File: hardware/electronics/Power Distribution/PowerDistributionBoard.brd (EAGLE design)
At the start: 128.3 x 50.8 mm, 74 parts, among them IC1 LM556D, IC2 74AHC1G02DBV, IC3 74AHC1G02DBV, K1 EC2-12TNU, U1 IPS6041G, U2 IPS6041G, U3 V_REG_317SMD

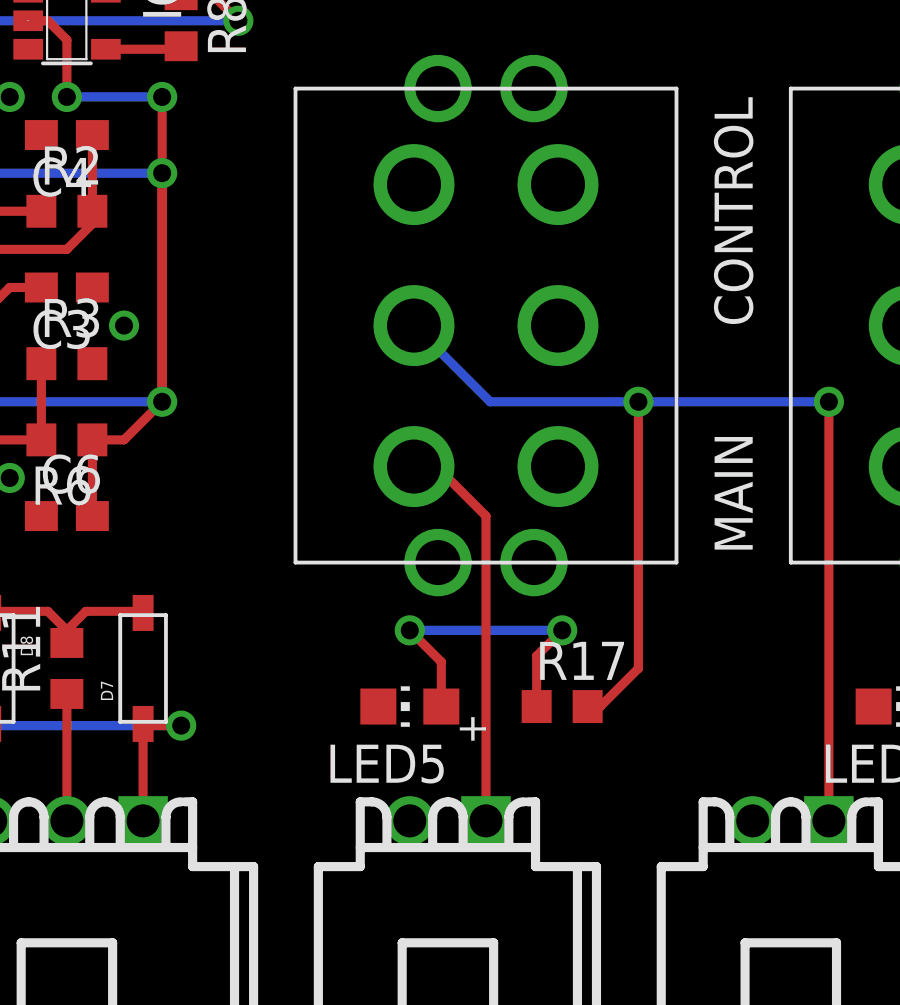
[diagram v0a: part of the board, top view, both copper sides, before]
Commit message: Changed the R/C input over to SBUS. Updates to the PowerDistributionBaord
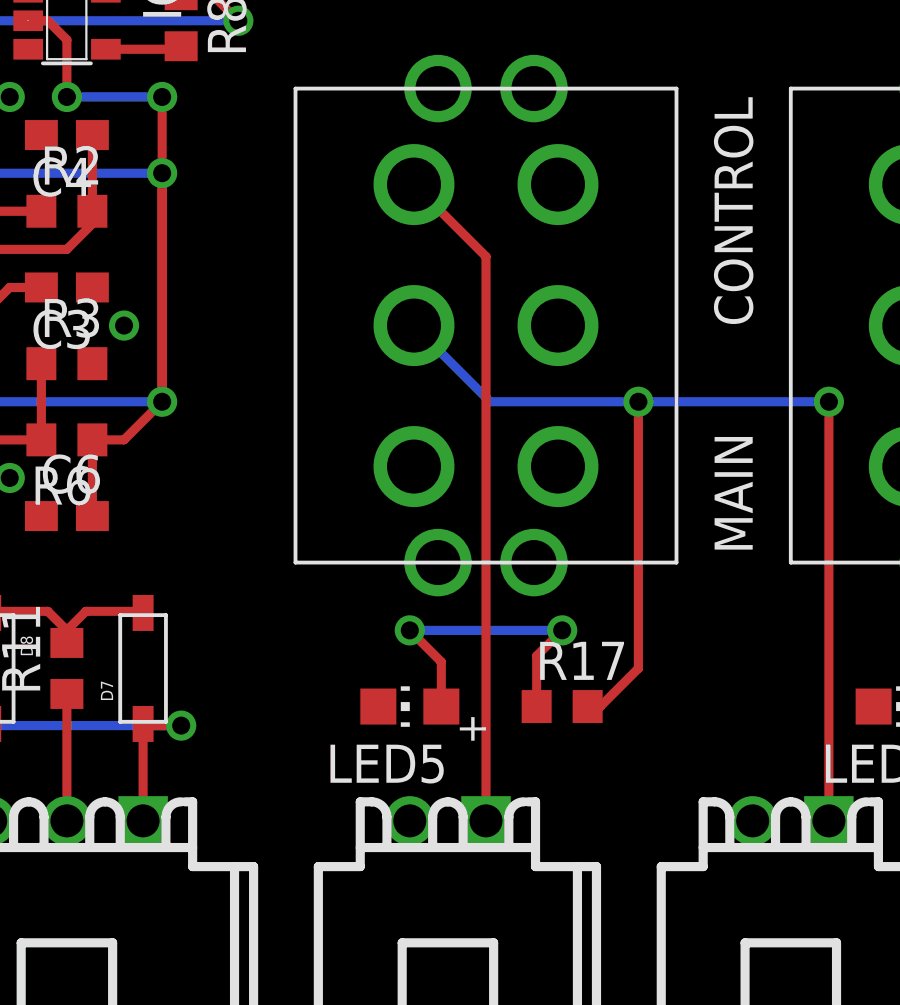
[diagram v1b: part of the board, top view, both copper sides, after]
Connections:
- net GND: now also CONTROL.3, CONTROL.6, HORN.3, HORN.6, MAIN.1, MAIN.6, MOTOR.3, MOTOR.6
- net N$34: now also MAIN.3; no longer MAIN.1
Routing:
- net N$34: track 13.2 -> 22.2 mm
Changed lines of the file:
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@@
 <contactref element="U3" pad="1"/>
 <contactref element="C10" pad="2"/>
-<contactref element="MAIN" pad="4"/>
 <contactref element="HORN" pad="4"/>
 <contactref element="CONTROL" pad="4"/>
@@
 <via x="51.435" y="30.48" extent="1-16" drill="0.6"/>
 <via x="47.625" y="25.4" extent="1-16" drill="0.6"/>
+<contactref element="MAIN" pad="6"/>
+<contactref element="CONTROL" pad="6"/>
+<contactref element="CONTROL" pad="3"/>
+<contactref element="MAIN" pad="4"/>
+<contactref element="MAIN" pad="1"/>
+<contactref element="MOTOR" pad="3"/>
+<contactref element="MOTOR" pad="6"/>
+<contactref element="HORN" pad="3"/>
+<contactref element="HORN" pad="6"/>
 </signal>
 <signal name="+5V">
@@
 </signal>
 <signal name="N$34">
-<contactref element="MAIN" pad="1"/>
 <contactref element="AUX-PWR" pad="P$1"/>
-<wire x1="63.5" y1="13.97" x2="63.5" y2="24.13" width="0.3048" layer="1"/>
-<wire x1="61.1" y1="25.78" x2="61.85" y2="25.78" width="0.3048" layer="1"/>
-<wire x1="61.85" y1="25.78" x2="63.5" y2="24.13" width="0.3048" layer="1"/>
+<wire x1="63.5" y1="13.97" x2="63.5" y2="32.78" width="0.3048" layer="1"/>
+<contactref element="MAIN" pad="3"/>
+<wire x1="63.5" y1="32.78" x2="61.1" y2="35.18" width="0.3048" layer="1"/>
 </signal>
 </signals>

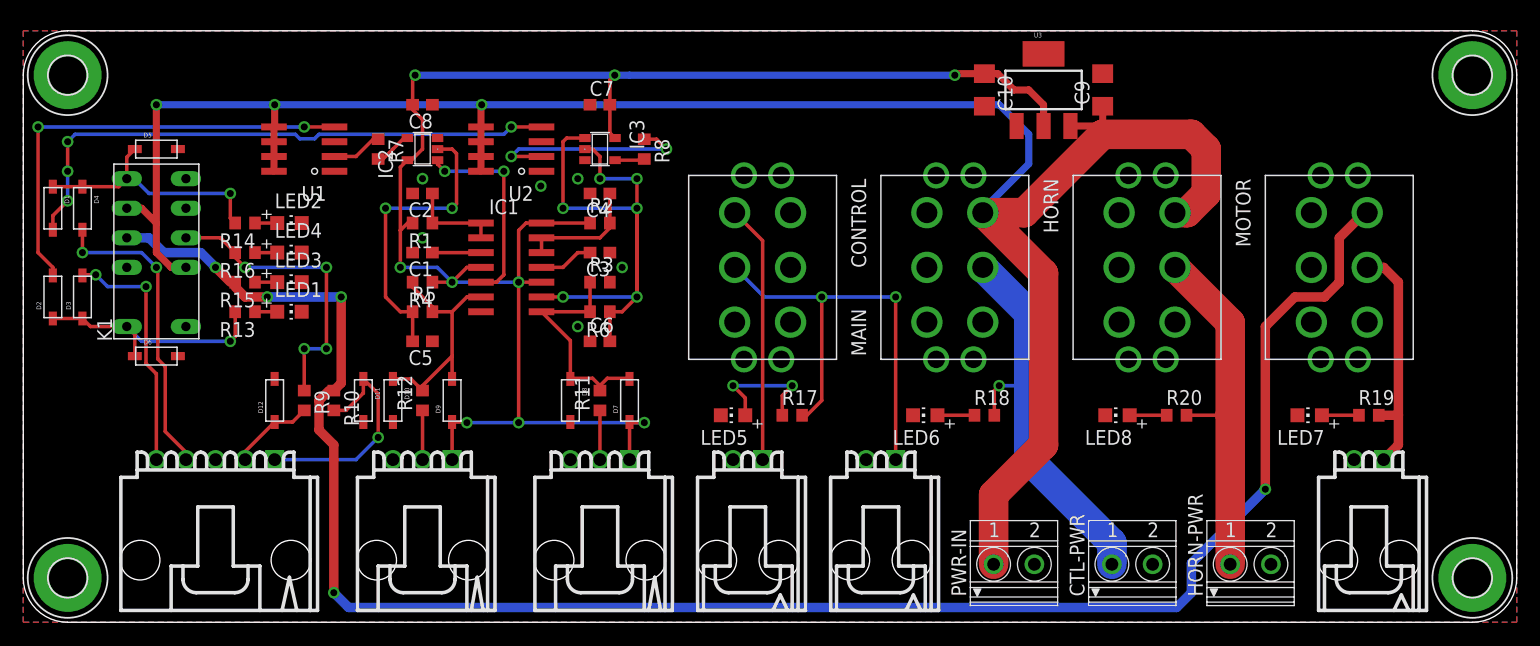
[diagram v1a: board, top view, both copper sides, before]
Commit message: Making sure we have the latest board in github
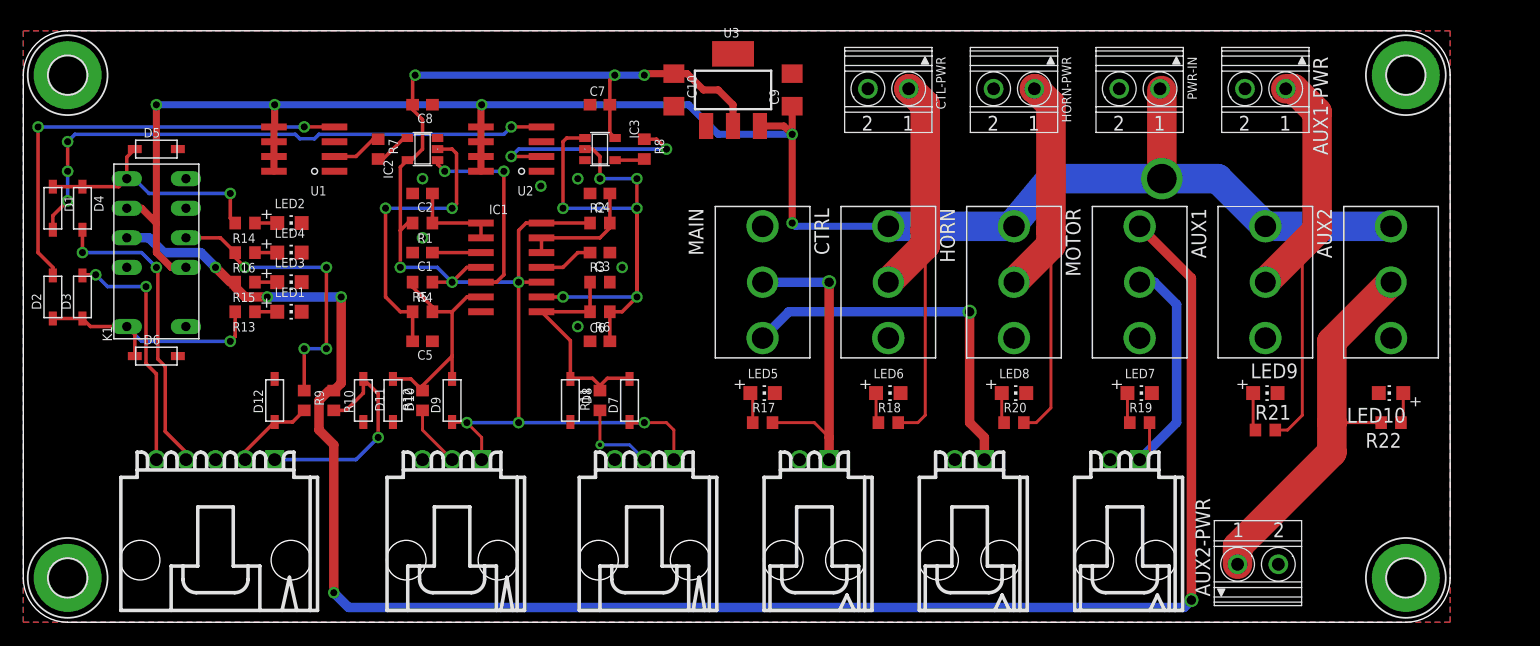
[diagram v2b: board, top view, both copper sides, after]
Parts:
- removed CONTROL: M20-DPDT, logos-switch:M20****13*
- added AUX1, AUX2, CTRL: M20-SPDT, logos-switch:M20-SPDT
- added AUX1-PWR, AUX2-PWR: 1751248, con-phoenix-350:1751248
- added LED10, LED9: (no value), adafruit:CHIP-LED0805
- added R21, R22: (no value), resistor:R0603
- HORN, MAIN, MOTOR: value M20-DPDT -> M20-SPDT; device logos-switch:M20****13* -> logos-switch:M20-SPDT
- moved CTL-PWR 45.7 mm to (74.3, 45.7), turned to 180 degrees
- moved HORN-PWR 45.4 mm to (85.1, 45.7), turned to 180 degrees
- moved PWR-IN 42.0 mm to (95.9, 45.7), turned to 180 degrees
- moved C10 26.7 mm to (55.9, 45.7)
- moved U3 26.7 mm to (61.0, 45.7)
- moved C9 26.7 mm to (66.0, 45.7)
- moved MOTOR-RELAY 21.0 mm to (94.6, 14.0)
- moved R19 19.7 mm to (95.9, 17.1)
- moved AUX-PWR 19.1 mm to (81.3, 14.0)
- moved MOTOR 17.2 mm to (95.9, 29.2)
- moved LED7 14.7 mm to (95.9, 19.7), turned to 270 degrees
- moved R20 14.0 mm to (85.1, 17.1)
- moved HORN 11.5 mm to (85.1, 29.2)
- moved LED8 9.09 mm to (85.1, 19.7), turned to 270 degrees
- moved R18 8.28 mm to (74.3, 17.1)
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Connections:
- new net N$29: AUX1-PWR.1, AUX1.2, R21.2
- new net N$31: LED9.A, R21.1
- new net N$37: AUX2-PWR.1, AUX2.2, R22.2
- new net N$39: LED10.A, R22.1
- net +12V: now also AUX1.1, AUX2.1, CTRL.1; no longer CONTROL.1
- net GND: now also AUX1-PWR.2, AUX1.3, AUX2-PWR.2, AUX2.3, CTRL.3, LED10.C, LED9.C; no longer CONTROL.3, CONTROL.4, CONTROL.5, CONTROL.6, CONTROL.G0, CONTROL.G1, CONTROL.G2, CONTROL.G3, HORN.4, HORN.5, HORN.6, HORN.G0, HORN.G1, HORN.G2, HORN.G3, MAIN.4, MAIN.5, MAIN.6, MAIN.G0, MAIN.G1, MAIN.G2, MAIN.G3, MOTOR.4, MOTOR.5, MOTOR.6, MOTOR.G0, MOTOR.G1, MOTOR.G2, MOTOR.G3
- net N$38: now also CTRL.2; no longer CONTROL.2
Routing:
- net N$29: track 0.00 -> 37.9 mm
- net N$37: track 0.00 -> 33.9 mm
- net +5V: track 146.5 -> 122.4 mm
- net +12V: track 183.9 -> 162.2 mm, vias 3 -> 6
- net N$41: track 40.0 -> 26.3 mm, vias 2 -> 1
- net N$34: track 22.2 -> 31.9 mm, vias 0 -> 1
- net N$32: track 10.9 -> 2.62 mm, vias 2 -> 0
- net ENABLE: track 163.0 -> 156.1 mm
- net N$33: track 31.2 -> 36.6 mm
- net N$31: track 0.00 -> 3.26 mm
- net N$26: track 4.23 -> 7.30 mm, vias 0 -> 1
- net N$39: track 0.00 -> 2.62 mm
- net N$38: track 35.3 -> 37.0 mm, vias 1 -> 0
- net N$36: track 20.7 -> 22.1 mm
- net N$25: track 4.23 -> 5.28 mm
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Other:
- board size 128.3 x 50.8 mm -> 122.6 x 50.8 mm

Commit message: A bit of BoM and silkscreen cleanup
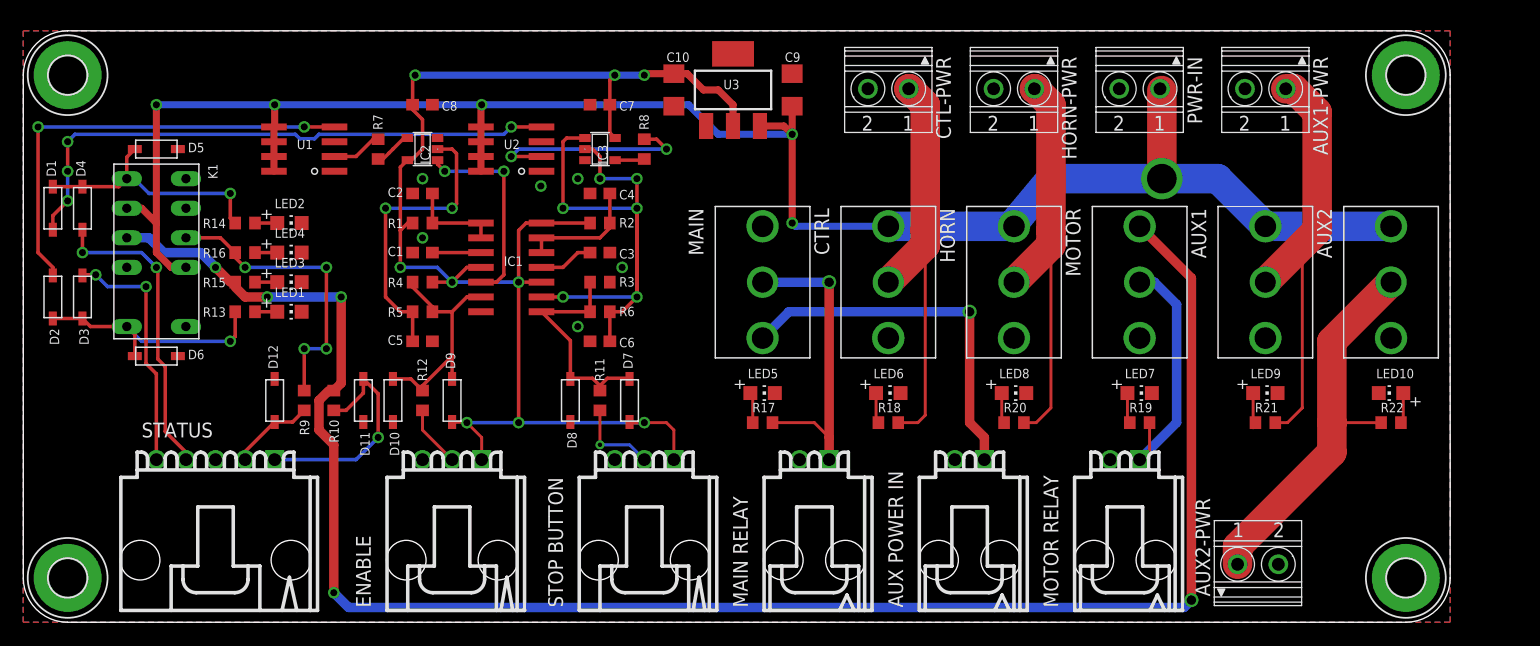
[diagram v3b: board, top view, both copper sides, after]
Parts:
- moved R21 0.63 mm to (106.7, 17.1)
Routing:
- net N$29: track 37.9 -> 37.2 mm
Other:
- board text added: "AUX POWER IN"
- board text added: "ENABLE"
- board text added: "MAIN RELAY"
- board text added: "MOTOR RELAY"
- board text added: "STATUS"
- board text added: "STOP BUTTON"
